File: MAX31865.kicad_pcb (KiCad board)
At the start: 2 copper layers, 25.4 x 27.9 mm, 29 parts, among them U1 MAX31865, U3 MIC5225-3.3, X1 3.5mm, X2 3.5mm

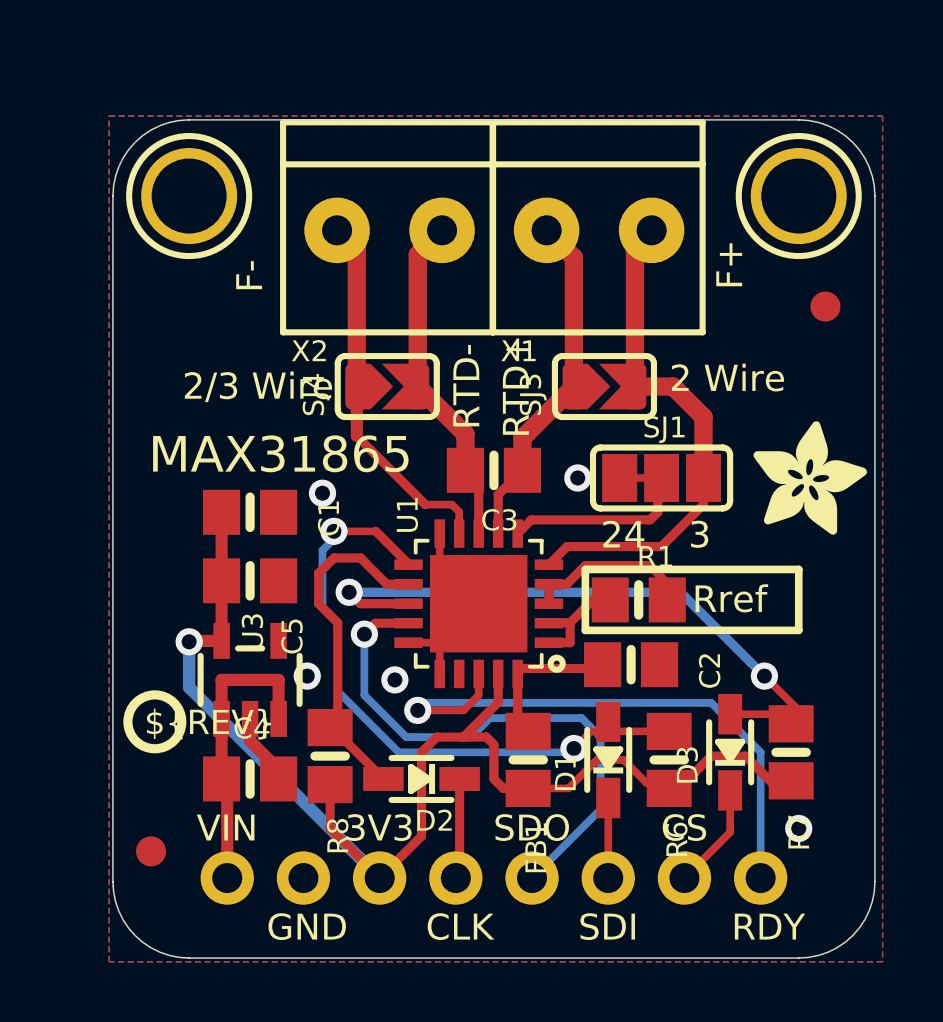
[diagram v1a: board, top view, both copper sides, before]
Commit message: changed all capacitor footprints on pcb layout
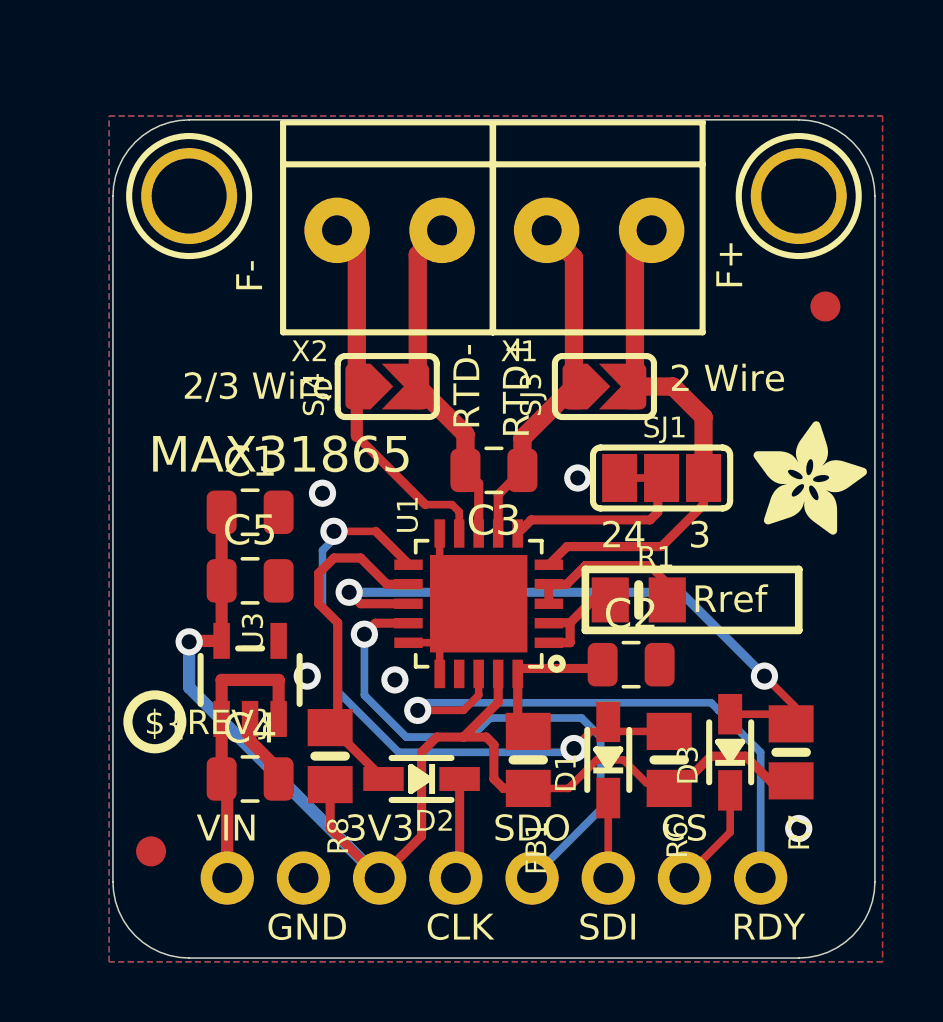
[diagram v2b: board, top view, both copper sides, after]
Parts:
- C1, C2, C3, C4, C5: footprint 0805-NO -> Capacitor_SMD:C_0805_2012Metric

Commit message: changed all diode footprints on pcb layout
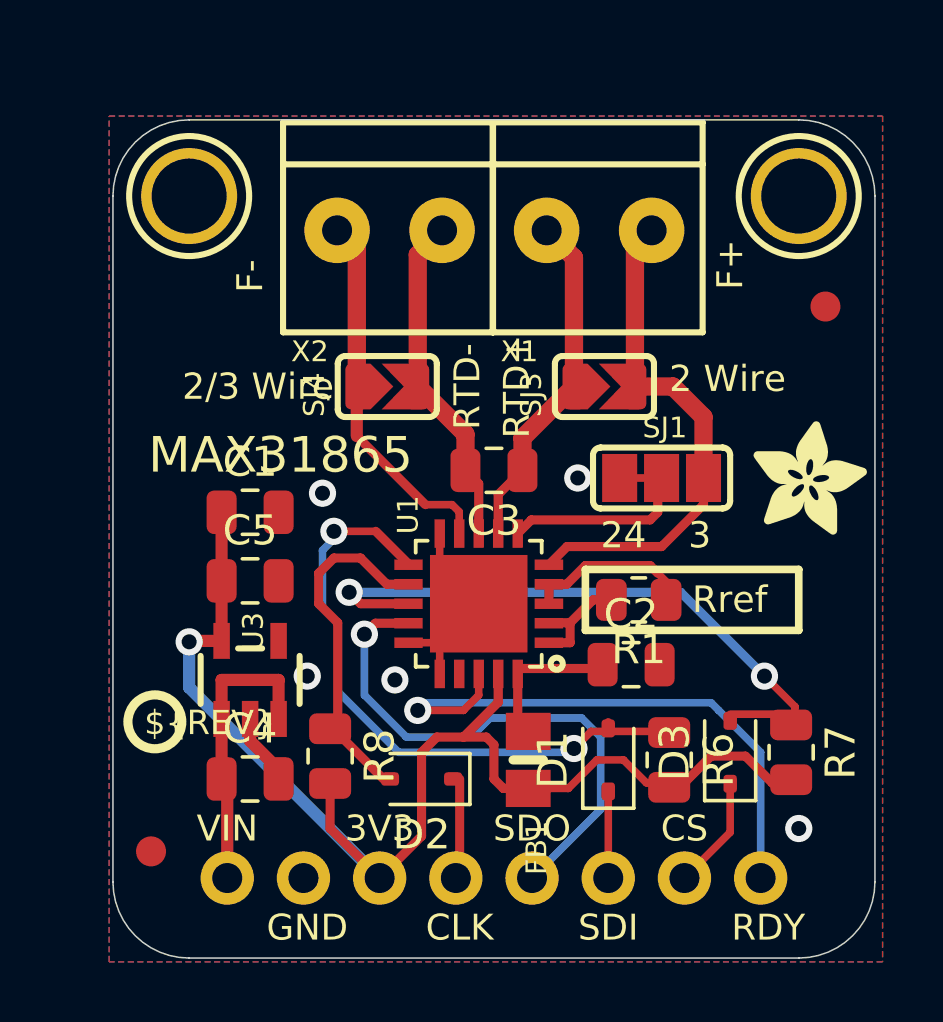
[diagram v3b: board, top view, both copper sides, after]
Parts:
- D1, D2, D3: footprint SOD-323 -> Diode_SMD:D_SOD-323
- R1, R6, R7, R8: footprint 0805-NO -> Resistor_SMD:R_0805_2012Metric

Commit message: changed all connector footprints on pcb layout
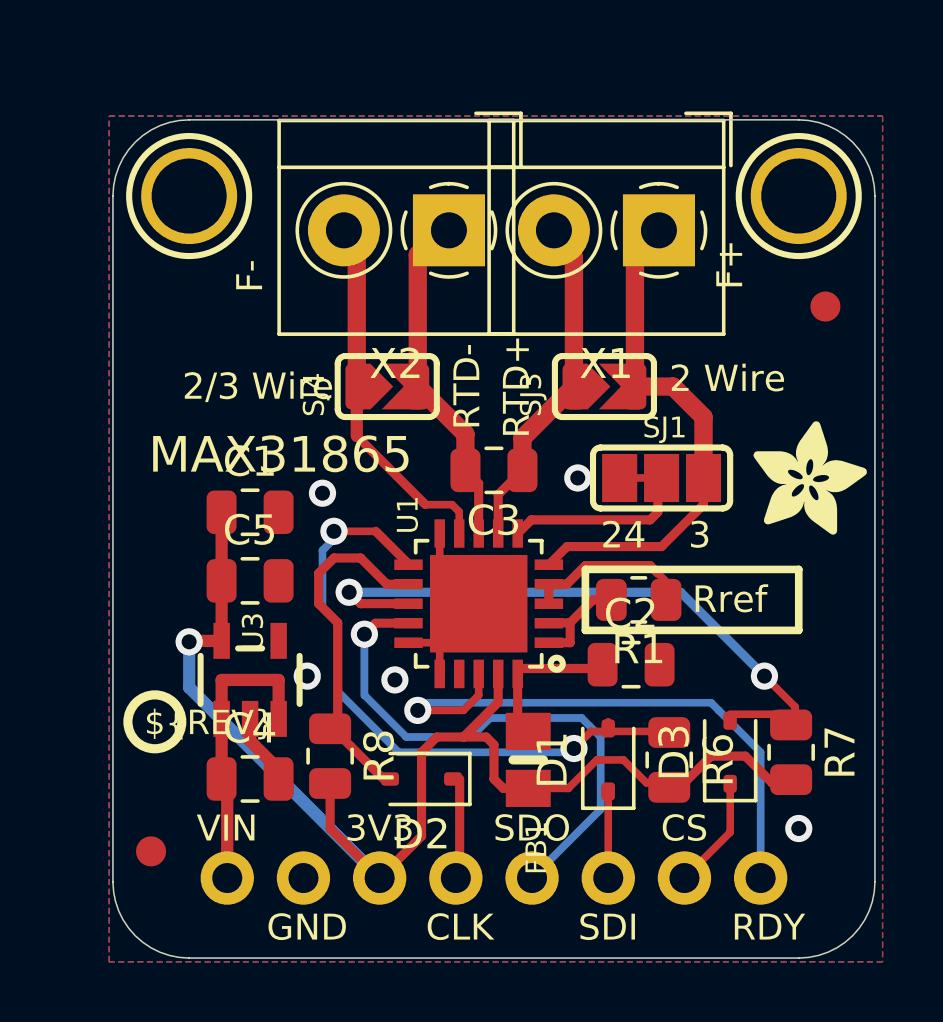
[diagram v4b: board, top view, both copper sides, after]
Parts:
- X1, X2: footprint TERMBLOCK_1X2-3.5MM -> TerminalBlock_4Ucon:TerminalBlock_4Ucon_1x02_P3.50mm_Horizontal
- moved X1 1.94 mm to (154.0, 94.7)
- moved X2 1.93 mm to (147.0, 94.7)

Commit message: changed connector pin 1x08 footprints on pcb layout
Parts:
- JP1: footprint 1X08_ROUND_70 -> Connector_PinHeader_2.54mm:PinHeader_1x08_P2.54mm_Vertical
- moved JP1 8.66 mm to (139.8, 116.5), turned to 90 degrees

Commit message: changed mounting hole footprint in schematic and pcb layout
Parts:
- U$18, U$19: footprint MOUNTINGHOLE_2.5_PLATED -> MountingHole:MountingHole_2.5mm

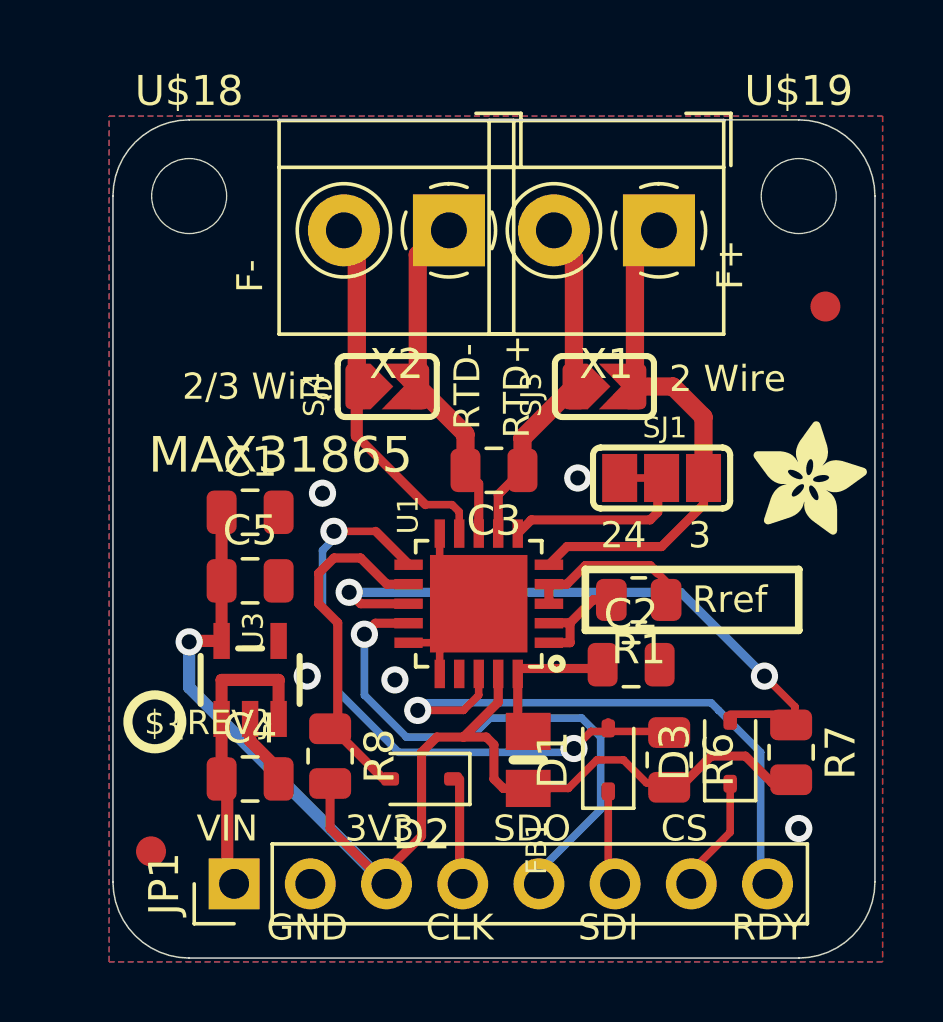
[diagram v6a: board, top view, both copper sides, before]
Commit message: changed solder footprint in schematic and pcb layout
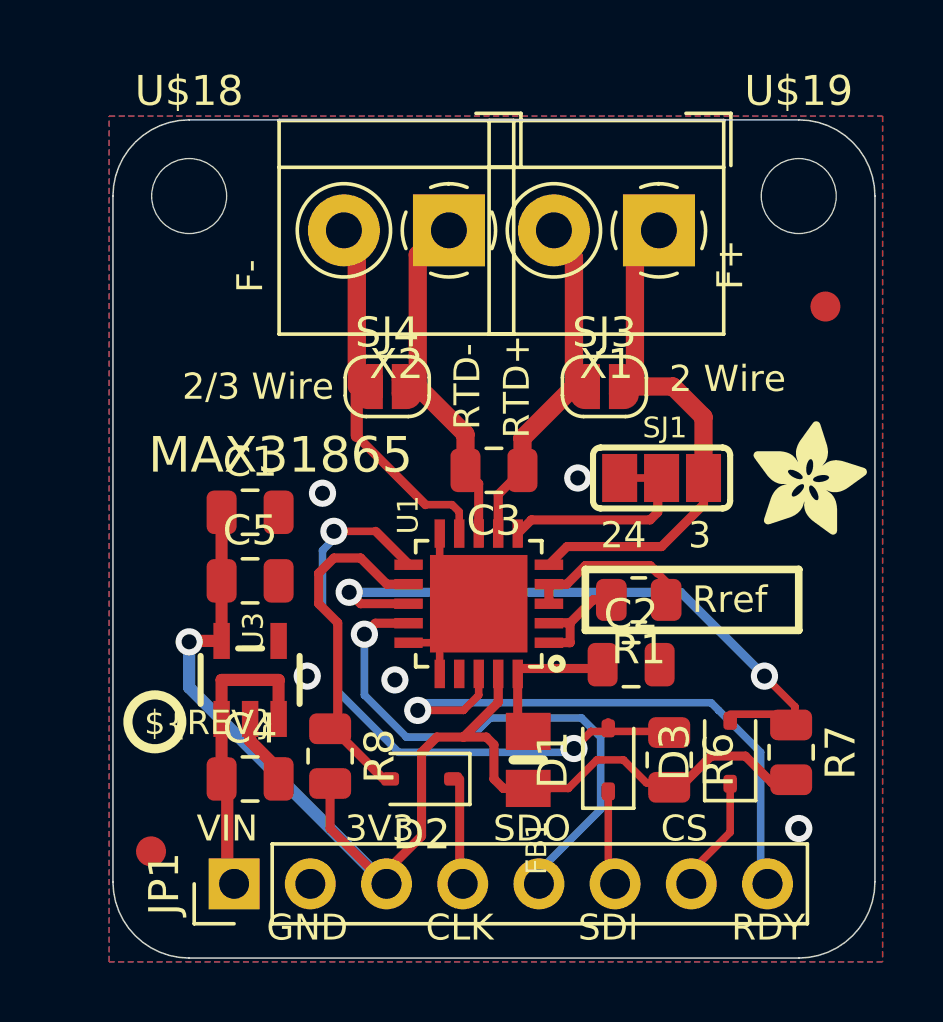
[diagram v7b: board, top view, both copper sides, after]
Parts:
- SJ3, SJ4: footprint SOLDERJUMPER_ARROW_NOPASTE -> Jumper:SolderJumper-2_P1.3mm_Open_RoundedPad1.0x1.5mm

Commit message: changed fiducial footprint in schematic and pcb layout
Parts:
- FID1, FID2: footprint FIDUCIAL_1MM -> Fiducial:Fiducial_1mm_Mask2mm
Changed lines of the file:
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@@
 		)
 	)
-	(footprint "FIDUCIAL_1MM"
+	(footprint "Fiducial:Fiducial_1mm_Mask2mm"
 		(layer "F.Cu")
 		(at 137.0711 115.4176 90)
+		(descr "Circular Fiducial, 1mm bare copper, 2mm soldermask opening (Level A)")
+		(tags "fiducial")
 		(property "Reference" "FID2"
-			(at 0 0 90)
-			(unlocked yes)
+			(at 0 -2 90)
 			(layer "F.SilkS")
-			(hide yes)
 			(effects
 				(font
-					(size 1.27 1.27)
+					(size 1 1)
+					(thickness 0.15)
 				)
-				(justify right top)
 			)
 		)
 		(property "Value" "FIDUCIAL\"\""
-			(at 0 0 90)
-			(unlocked yes)
+			(at 0 2 90)
 			(layer "F.Fab")
-			(hide yes)
 			(effects
 				(font
-					(size 1.27 1.27)
+					(size 1 1)
+					(thickness 0.15)
 				)
-				(justify right top)
 			)
 		)
@@
 			)
 		)
-		(fp_arc
-			(start 0 -0.75)
-			(mid 0.53033 -0.53033)
-			(end 0.75 0)
-			(stroke
-				(width 0.5)
-				(type solid)
-			)
-			(layer "F.Mask")
-		)
-		(fp_arc
-			(start 0.75 0)
-			(mid 0.53033 0.53033)
-			(end 0 0.75)
-			(stroke
-				(width 0.5)
-				(type solid)
-			)
-			(layer "F.Mask")
-		)
-		(fp_arc
-			(start -0.75 0)
-			(mid -0.53033 -0.53033)
-			(end 0 -0.75)
-			(stroke
-				(width 0.5)
-				(type solid)
-			)
-			(layer "F.Mask")
-		)
-		(fp_arc
-			(start 0 0.75)
-			(mid -0.53033 0.53033)
-			(end -0.75 0)
-			(stroke
-				(width 0.5)
-				(type solid)
-			)
-			(layer "F.Mask")
-		)
-		(fp_arc
-			(start 0 -0.75)
-			(mid 0.53033 -0.53033)
-			(end 0.75 0)
-			(stroke
-				(width 0.5)
-				(type solid)
-			)
-			(layer "F.CrtYd")
-		)
-		(fp_arc
-			(start 0.75 0)
-			(mid 0.53033 0.53033)
-			(end 0 0.75)
+		(attr smd)
+		(fp_circle
+			(center 0 0)
+			(end 1.25 0)
 			(stroke
-				(width 0.5)
+				(width 0.05)
 				(type solid)
 			)
+			(fill none)
 			(layer "F.CrtYd")
 		)
-		(fp_arc
-			(start -0.75 0)
-			(mid -0.53033 -0.53033)
-			(end 0 -0.75)
+		(fp_circle
+			(center 0 0)
+			(end 1 0)
 			(stroke
-				(width 0.5)
+				(width 0.1)
 				(type solid)
 			)
-			(layer "F.CrtYd")
+			(fill none)
+			(layer "F.Fab")
 		)
-		(fp_arc
-			(start 0 0.75)
-			(mid -0.53033 0.53033)
-			(end -0.75 0)
-			(stroke
-				(width 0.5)
-				(type solid)
+		(fp_text user "${REFERENCE}"
+			(at 0 0 90)
+			(layer "F.Fab")
+			(effects
+				(font
+					(size 0.4 0.4)
+					(thickness 0.06)
+				)
 			)
-			(layer "F.CrtYd")
 		)
-		(pad "1" smd roundrect
+		(pad "" smd circle
 			(at 0 0 90)
 			(size 1 1)
 			(layers "F.Cu" "F.Mask")
-			(roundrect_rratio 0.5)
-			(solder_mask_margin 0.0508)
-			(thermal_bridge_angle 0)
+			(solder_mask_margin 0.5)
+			(clearance 0.5)
 		)
 	)
@@
 		)
 	)
-	(footprint "FIDUCIAL_1MM"
+	(footprint "Fiducial:Fiducial_1mm_Mask2mm"
 		(layer "F.Cu")
 		(at 159.5501 97.2566 90)
+		(descr "Circular Fiducial, 1mm bare copper, 2mm soldermask opening (Level A)")
+		(tags "fiducial")
 		(property "Reference" "FID1"
-			(at 0 0 90)
-			(unlocked yes)
+			(at 0 -2 90)
 			(layer "F.SilkS")
-			(hide yes)
 			(effects
 				(font
-					(size 1.27 1.27)
+					(size 1 1)
+					(thickness 0.15)
 				)
-				(justify right top)
 			)
 		)
 		(property "Value" "FIDUCIAL\"\""
-			(at 0 0 90)
-			(unlocked yes)
+			(at 0 2 90)
 			(layer "F.Fab")
-			(hide yes)
 			(effects
 				(font
-					(size 1.27 1.27)
+					(size 1 1)
+					(thickness 0.15)
 				)
-				(justify right top)
 			)
 		)
@@
 			)
 		)
-		(fp_arc
-			(start 0 -0.75)
-			(mid 0.53033 -0.53033)
-			(end 0.75 0)
-			(stroke
-				(width 0.5)
-				(type solid)
-			)
-			(layer "F.Mask")
-		)
-		(fp_arc
-			(start 0.75 0)
-			(mid 0.53033 0.53033)
-			(end 0 0.75)
-			(stroke
-				(width 0.5)
-				(type solid)
-			)
-			(layer "F.Mask")
-		)
-		(fp_arc
-			(start -0.75 0)
-			(mid -0.53033 -0.53033)
-			(end 0 -0.75)
-			(stroke
-				(width 0.5)
-				(type solid)
-			)
-			(layer "F.Mask")
-		)
-		(fp_arc
-			(start 0 0.75)
-			(mid -0.53033 0.53033)
-			(end -0.75 0)
-			(stroke
-				(width 0.5)
-				(type solid)
-			)
-			(layer "F.Mask")
-		)
-		(fp_arc
-			(start 0 -0.75)
-			(mid 0.53033 -0.53033)
-			(end 0.75 0)
-			(stroke
-				(width 0.5)
-				(type solid)
-			)
-			(layer "F.CrtYd")
-		)
-		(fp_arc
-			(start 0.75 0)
-			(mid 0.53033 0.53033)
-			(end 0 0.75)
+		(attr smd)
+		(fp_circle
+			(center 0 0)
+			(end 1.25 0)
 			(stroke
-				(width 0.5)
+				(width 0.05)
 				(type solid)
 			)
+			(fill none)
 			(layer "F.CrtYd")
 		)
-		(fp_arc
-			(start -0.75 0)
-			(mid -0.53033 -0.53033)
-			(end 0 -0.75)
+		(fp_circle
+			(center 0 0)
+			(end 1 0)
 			(stroke
-				(width 0.5)
+				(width 0.1)
 				(type solid)
 			)
-			(layer "F.CrtYd")
+			(fill none)
+			(layer "F.Fab")
 		)
-		(fp_arc
-			(start 0 0.75)
-			(mid -0.53033 0.53033)
-			(end -0.75 0)
-			(stroke
-				(width 0.5)
-				(type solid)
+		(fp_text user "${REFERENCE}"
+			(at 0 0 90)
+			(layer "F.Fab")
+			(effects
+				(font
+					(size 0.4 0.4)
+					(thickness 0.06)
+				)
 			)
-			(layer "F.CrtYd")
 		)
-		(pad "1" smd roundrect
+		(pad "" smd circle
 			(at 0 0 90)
 			(size 1 1)
 			(layers "F.Cu" "F.Mask")
-			(roundrect_rratio 0.5)
-			(solder_mask_margin 0.0508)
-			(thermal_bridge_angle 0)
+			(solder_mask_margin 0.5)
+			(clearance 0.5)
 		)
 	)
